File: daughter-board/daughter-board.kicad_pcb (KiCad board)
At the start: 2 copper layers, 48.5 x 12.8 mm, 5 parts, among them J1 USB-C Connector, J2 Conn_01x08, P1 IPOD_CONNECTOR_MALE

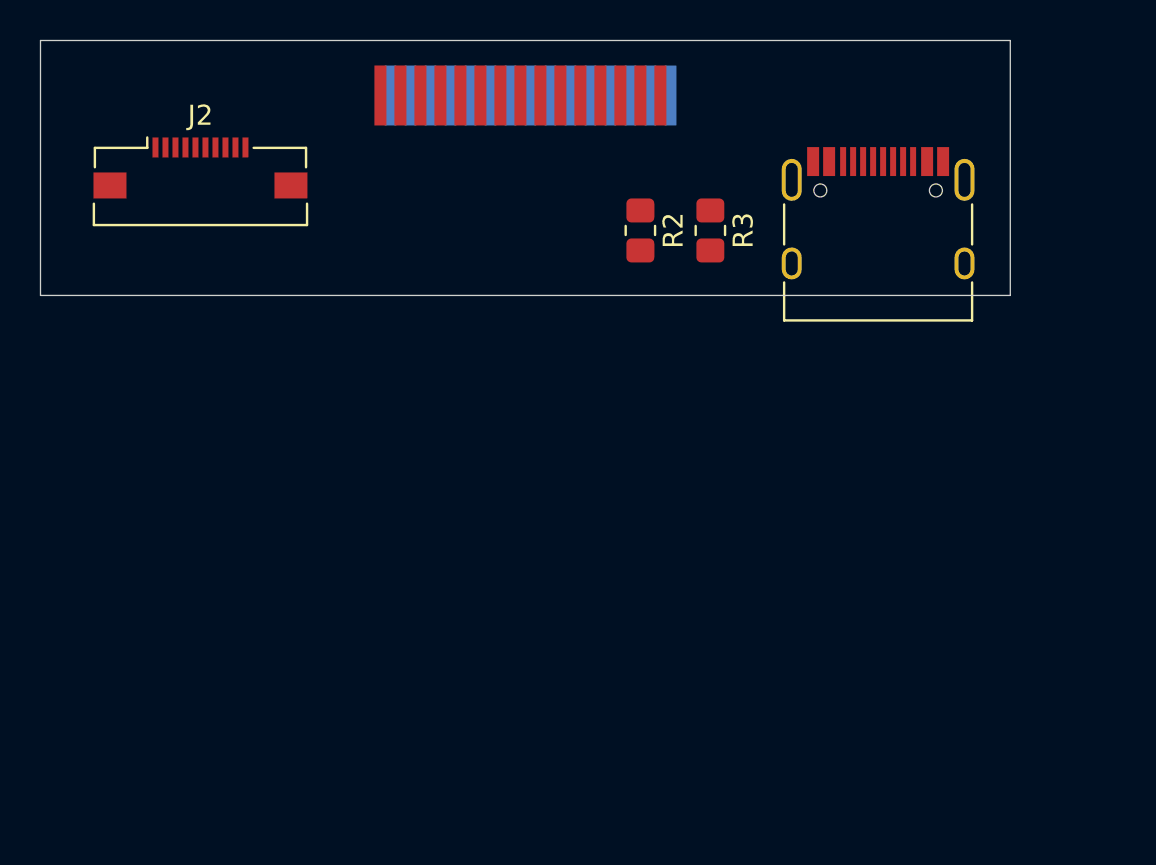
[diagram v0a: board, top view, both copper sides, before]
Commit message: Change FFC to match fab house.
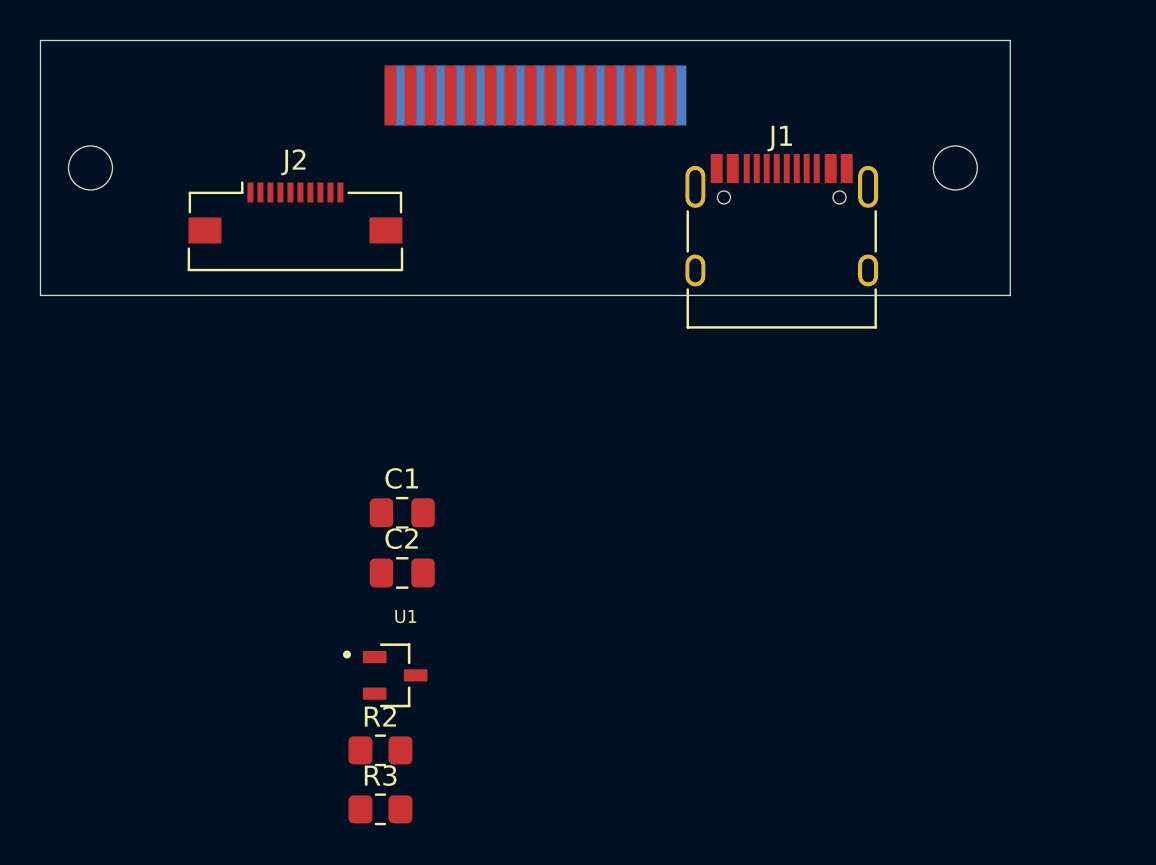
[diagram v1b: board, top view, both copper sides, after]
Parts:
- added C1: 0.1uF, Capacitor_SMD:C_0805_2012Metric_Pad1.18x1.45mm_HandSolder, F.Cu at (169.8, 111.4)
- added C2: 0.1uF, Capacitor_SMD:C_0805_2012Metric_Pad1.18x1.45mm_HandSolder, F.Cu at (169.8, 114.4)
- added REF**: MountingHole_2.2mm_M2, MountingHole:MountingHole_2.2mm_M2, F.Cu at (154.2, 94.1)
- added REF**: MountingHole_2.2mm_M2, MountingHole:MountingHole_2.2mm_M2, F.Cu at (197.5, 94.1)
- added U1: AP2331SA-7, AP2331SA:SOT91P240X120-3N, F.Cu at (169.5, 119.5)
- J2: value Conn_01x08 -> Ribbon Connector
- moved R3 33.3 mm to (168.8, 126.2), turned to 0 degrees
- moved R2 29.1 mm to (168.8, 123.2), turned to 0 degrees
- moved J2 5.26 mm to (164.5, 96.4)
- moved J1 4.83 mm to (188.8, 98.2)
- moved P1 0.50 mm to (176.2, 90.5)
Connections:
- J2 pad 10: (no net) -> +5V
- J2 pad 3: ACC -> OUT_R
- J2 pad 4: D+ -> OUT_L
- J2 pad 5: D- -> ACC
- J2 pad 6: RX -> D+
- J2 pad 7: TX -> D-
- J2 pad 8: +5V -> RX
- J2 pad 9: (no net) -> TX
- P1 pad 11: unconnected-(P1-GND@11-Pad11) -> GNDS

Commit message: FFC routing
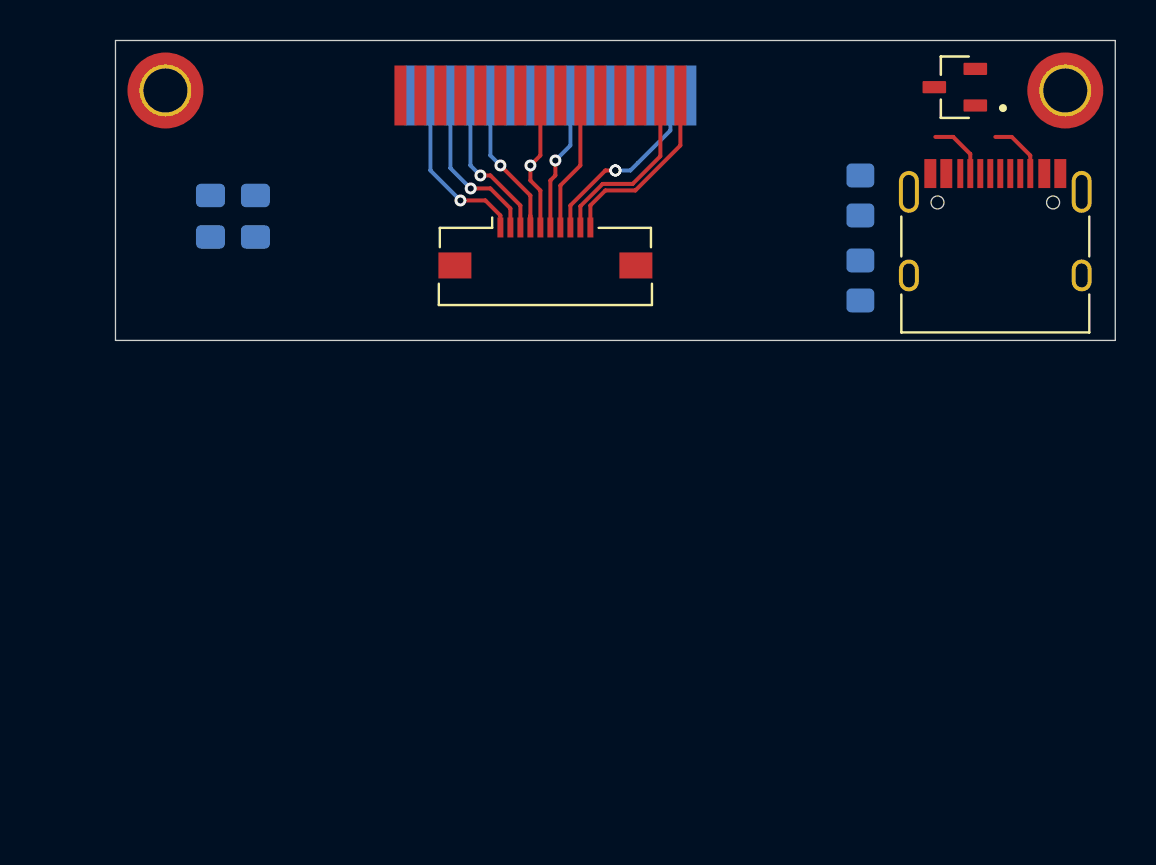
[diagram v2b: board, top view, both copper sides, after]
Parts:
- removed R3: 5K1, Resistor_SMD:R_0805_2012Metric_Pad1.20x1.40mm_HandSolder
- added R1: 5K1, Resistor_SMD:R_0805_2012Metric_Pad1.20x1.40mm_HandSolder, B.Cu at (192.8, 99.8)
- C1, C2, R2: moved to B.Cu
- REF** (x2): value MountingHole_2.2mm_M2 -> MountingHole_2.2mm_M2_DIN965_Pad_TopOnly; footprint MountingHole:MountingHole_2.2mm_M2 -> MountingHole:MountingHole_2.2mm_M2_DIN965_Pad_TopOnly
- moved U1 40.6 mm to (197.5, 90.1), turned to 180 degrees
- moved R2 36.7 mm to (192.8, 95.5), turned to -90 degrees
- moved C2 19.3 mm to (162.5, 96.5), turned to -90 degrees
- moved C1 17.7 mm to (160.2, 96.5), turned to -90 degrees
- moved J2 12.6 mm to (177.0, 98.1)
- moved J1 10.7 mm to (199.5, 98.5)
- moved REF** 6.73 mm to (203.0, 90.2)
- moved REF** 5.39 mm to (158.0, 90.2)
- moved P1 0.50 mm to (176.8, 90.5)
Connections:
- J2 pad 1: GNDS -> D+
- J2 pad 10: +5V -> GNDA
- J2 pad 2: GNDA -> D-
- J2 pad 3: OUT_R -> +5V
- J2 pad 4: OUT_L -> ACC
- J2 pad 5: ACC -> GNDS
- J2 pad 6: D+ -> RX
- J2 pad 7: D- -> TX
- J2 pad 8: RX -> OUT_R
- J2 pad 9: TX -> OUT_L
- R2 pad 1: Net-(J1-CC2) -> Net-(J1-CC1)
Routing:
- net OUT_R: track 0.00 -> 9.40 mm, vias 0 -> 2
- net GNDA: track 0.00 -> 9.34 mm
- net OUT_L: track 0.00 -> 9.14 mm
- net D+: track 0.00 -> 8.78 mm, vias 0 -> 1
- net D-: track 0.00 -> 8.42 mm, vias 0 -> 1
- net ACC: track 0.00 -> 8.03 mm, vias 0 -> 1
- net +5V: track 0.00 -> 7.93 mm, vias 0 -> 1
- net RX: track 0.00 -> 7.01 mm, vias 0 -> 1
- net TX: track 0.00 -> 7.01 mm
- net GNDS: track 0.00 -> 7.01 mm, vias 0 -> 1
- net Net-(J1-CC2): track 0.00 -> 3.11 mm
- net Net-(J1-CC1): track 0.00 -> 3.08 mm
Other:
- board size 48.5 x 12.8 mm -> 50 x 15 mm

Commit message: Eh, not sure about this.
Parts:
- J1, J2, U1: moved to B.Cu
- REF** (x2): value MountingHole_2.2mm_M2_DIN965_Pad_TopOnly -> MountingHole_2.2mm_M2; footprint MountingHole:MountingHole_2.2mm_M2_DIN965_Pad_TopOnly -> MountingHole:MountingHole_2.2mm_M2
- moved R2 34.5 mm to (158.5, 99.8), turned to 180 degrees
- moved R1 34.5 mm to (158.5, 95.8), turned to 180 degrees
- moved J1 32.9 mm to (166.7, 98.5), turned to 180 degrees
- moved U1 23.2 mm to (174.2, 90.2)
- moved C1 15.8 mm to (175.8, 99.5), turned to 0 degrees
- moved C2 13.3 mm to (175.8, 95.2), turned to 0 degrees
- moved P1 10.8 mm to (187.5, 91.2)
- moved J2 10.8 mm to (187.8, 98.8), turned to 180 degrees
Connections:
- J2 pad 1: D+ -> GNDA
- J2 pad 10: GNDA -> D+
- J2 pad 2: D- -> OUT_R
- J2 pad 3: +5V -> OUT_L
- J2 pad 4: ACC -> TX
- J2 pad 5: GNDS -> RX
- J2 pad 6: RX -> GNDS
- J2 pad 7: TX -> ACC
- J2 pad 8: OUT_R -> +5V
- J2 pad 9: OUT_L -> D-
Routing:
- net Net-(U1-IN): track 0.00 -> 16.3 mm
- net Net-(J1-CC1): track 3.08 -> 11.2 mm
- net GNDA: track 9.34 -> 15.1 mm, vias 0 -> 1
- net Net-(J1-CC2): track 3.11 -> 8.63 mm
- net +5V: track 7.93 -> 12.0 mm, vias 1 -> 0
- net GNDS: track 7.01 -> 8.22 mm
- net D+: track 8.78 -> 8.05 mm, vias 1 -> 0
- net TX: track 7.01 -> 7.71 mm, vias 0 -> 1
- net ACC: track 8.03 -> 7.43 mm, vias 1 -> 0
- net D-: track 8.42 -> 7.84 mm, vias 1 -> 0
- net OUT_R: track 9.40 -> 8.90 mm, vias 2 -> 0
- net OUT_L: track 9.14 -> 8.90 mm, vias 0 -> 1
- net RX: vias 1 -> 0
